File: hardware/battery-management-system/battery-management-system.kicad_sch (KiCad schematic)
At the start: 4 parts

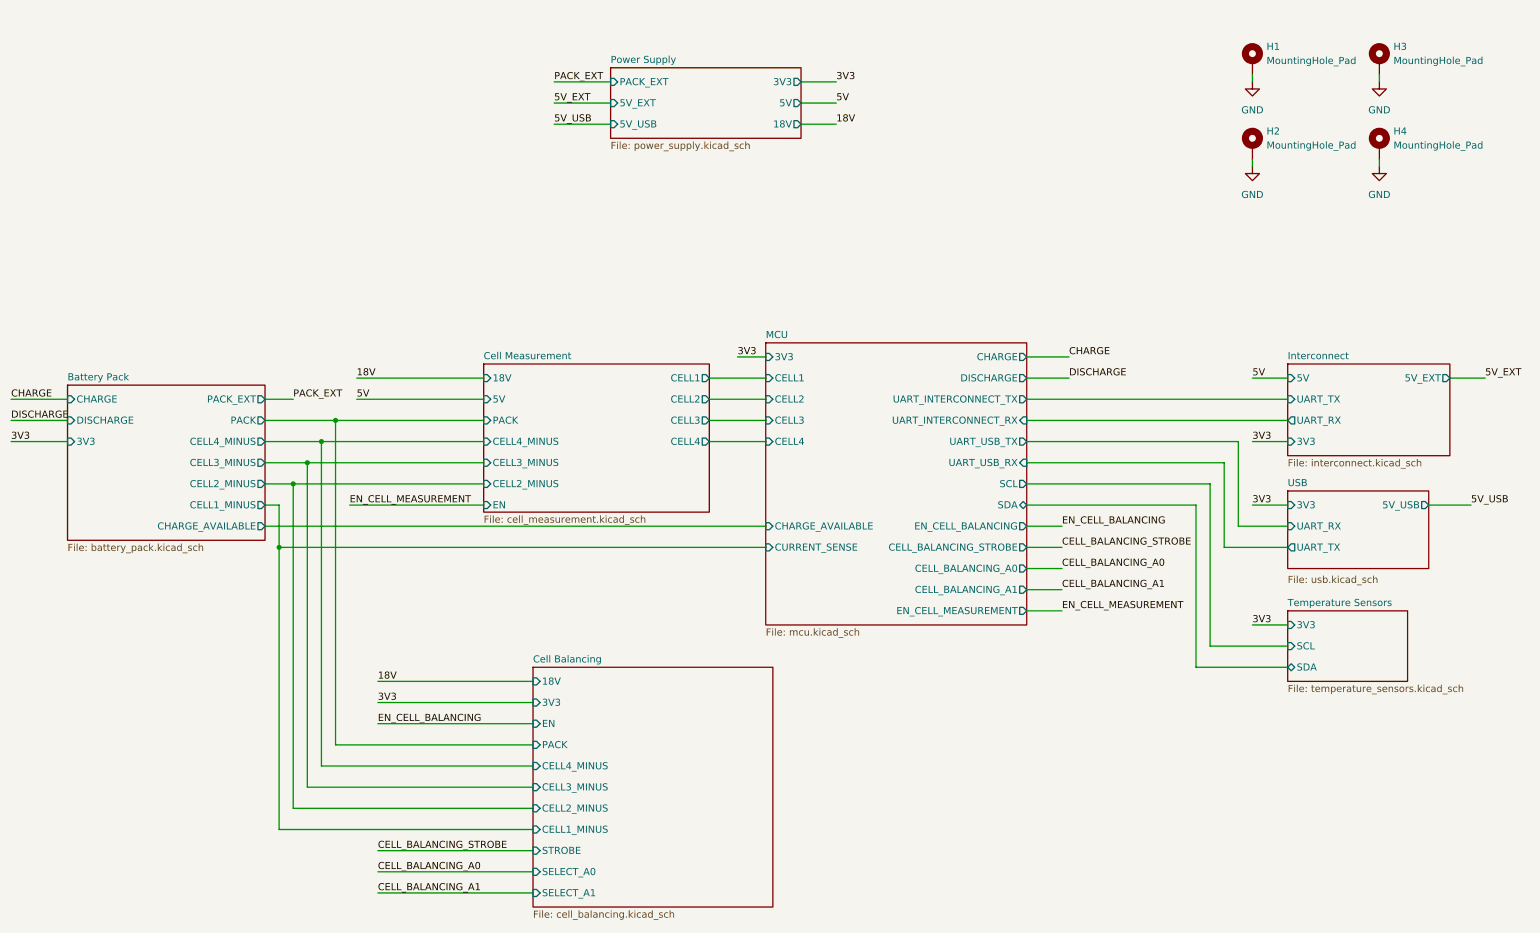
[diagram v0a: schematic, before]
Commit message: start simplifying BMS for R02
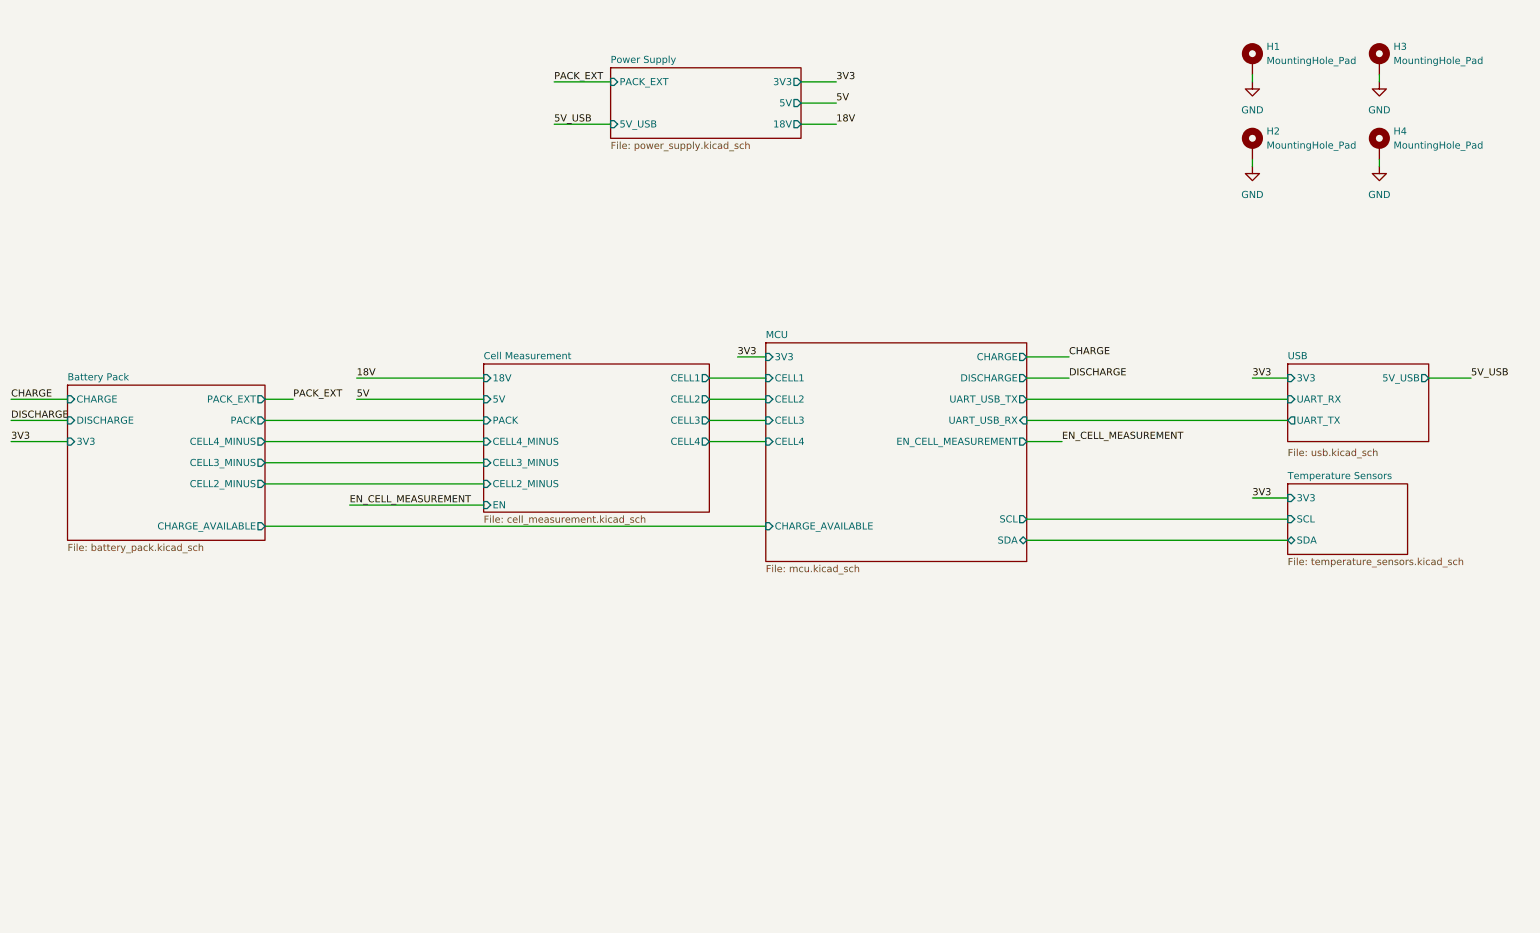
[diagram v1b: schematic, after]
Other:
- removed sheet Cell Balancing
- removed sheet Interconnect
- sheet Battery Pack ports: added none; removed CELL1_MINUS
- sheet MCU ports: added none; removed CELL_BALANCING_A0, CELL_BALANCING_A1, CELL_BALANCING_STROBE, CURRENT_SENSE, EN_CELL_BALANCING, UART_INTERCONNECT_RX, UART_INTERCONNECT_TX
- sheet Power Supply ports: added none; removed 5V_EXT

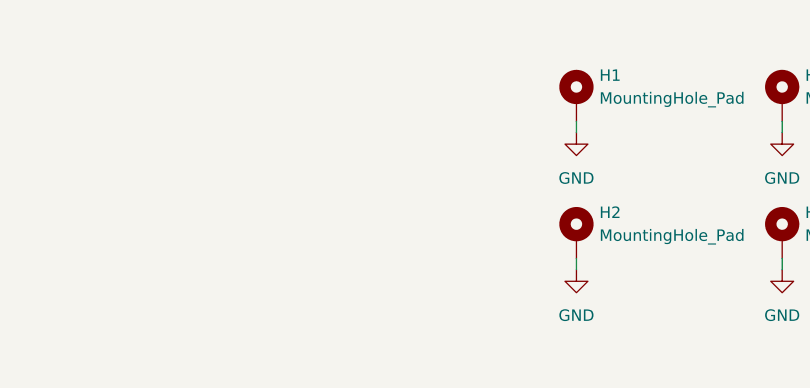
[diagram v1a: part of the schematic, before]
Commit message: add heatsink and fix ERC errors
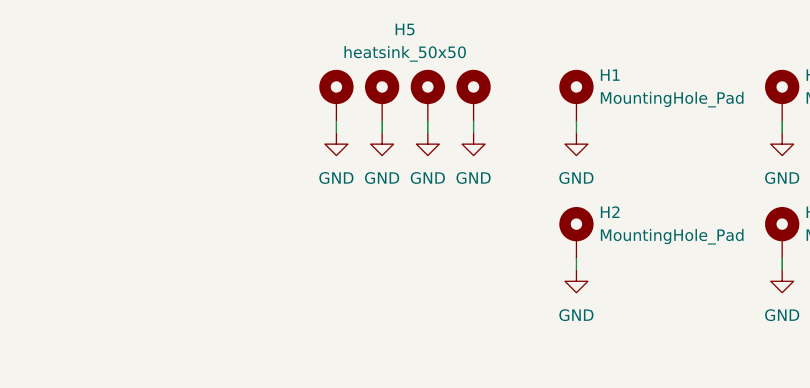
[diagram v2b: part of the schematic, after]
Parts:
- added H5: heatsink_50x50, benediktibk:heatsink_50x50, symbol benediktibk:heatsink_50x50
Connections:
- net GND: now also H5.1 (GND), H5.2 (GND), H5.3 (GND), H5.4 (GND)
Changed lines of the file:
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@@
+    (stroke (width 0) (type default))
+  )
+  (wire (pts (xy 209.55 25.4) (xy 209.55 26.67))
     (stroke (width 0) (type default))
   )
@@
     (stroke (width 0) (type default))
   )
+  (wire (pts (xy 219.71 25.4) (xy 219.71 26.67))
+    (stroke (width 0) (type default))
+  )
   (wire (pts (xy 74.93 80.01) (xy 97.79 80.01))
     (stroke (width 0) (type default))
@@
     (stroke (width 0) (type default))
   )
+  (wire (pts (xy 214.63 25.4) (xy 214.63 26.67))
+    (stroke (width 0) (type default))
+  )
   (wire (pts (xy 195.58 76.2) (xy 203.2 76.2))
     (stroke (width 0) (type default))
@@
     (stroke (width 0) (type default))
   )
+  (wire (pts (xy 224.79 25.4) (xy 224.79 26.67))
+    (stroke (width 0) (type default))
+  )
   (wire (pts (xy 195.58 83.82) (xy 242.57 83.82))
     (stroke (width 0) (type default))
@@
     )
   )
+  (symbol (lib_id "power:GND") (at 209.55 26.67 0) (unit 1)
+    (in_bom yes) (on_board yes) (dnp no) (fields_autoplaced)
+    (property "Reference" "#PWR067" (at 209.55 33.02 0)
+      (effects (font (size 1.27 1.27)) hide)
+    )
+    (property "Value" "GND" (at 209.55 31.75 0)
+      (effects (font (size 1.27 1.27)))
+    )
+    (property "Footprint" "" (at 209.55 26.67 0)
+      (effects (font (size 1.27 1.27)) hide)
+    )
+    (property "Datasheet" "" (at 209.55 26.67 0)
+      (effects (font (size 1.27 1.27)) hide)
+    )
+    (pin "1")
+    (instances
+      (project "battery-management-system"
+        (path "/5272f0ff-3069-41a9-bca2-80beede8b4b2"
+          (reference "#PWR067") (unit 1)
+        )
+      )
+    )
+  )
+  (symbol (lib_id "benediktibk:heatsink_50x50") (at 217.17 22.86 0) (unit 1)
+    (in_bom yes) (on_board yes) (dnp no) (fields_autoplaced)
+    (property "Reference" "H5" (at 217.17 15.24 0)
+      (effects (font (size 1.27 1.27)))
+    )
+    (property "Value" "heatsink_50x50" (at 217.17 17.78 0)
+      (effects (font (size 1.27 1.27)))
+    )
+    (property "Footprint" "benediktibk:heatsink_50x50" (at 217.297 12.954 0)
+      (effects (font (size 1.27 1.27)) hide)
+    )
+    (property "Datasheet" "~" (at 217.17 15.24 0)
+      (effects (font (size 1.27 1.27)) hide)
+    )
+    (pin "4")
+    (pin "1")
+    (pin "3")
+    (pin "2")
+    (instances
+      (project "battery-management-system"
+        (path "/5272f0ff-3069-41a9-bca2-80beede8b4b2"
+          (reference "H5") (unit 1)
+        )
+      )
+    )
+  )
   (symbol (lib_id "benediktibk:MountingHole_Pad_M6") (at 236.22 38.1 0) (unit 1)
     (in_bom yes) (on_board yes) (dnp no) (fields_autoplaced)
@@
     )
   )
+  (symbol (lib_id "power:GND") (at 224.79 26.67 0) (unit 1)
+    (in_bom yes) (on_board yes) (dnp no) (fields_autoplaced)
+    (property "Reference" "#PWR070" (at 224.79 33.02 0)
+      (effects (font (size 1.27 1.27)) hide)
+    )
+    (property "Value" "GND" (at 224.79 31.75 0)
+      (effects (font (size 1.27 1.27)))
+    )
+    (property "Footprint" "" (at 224.79 26.67 0)
+      (effects (font (size 1.27 1.27)) hide)
+    )
+    (property "Datasheet" "" (at 224.79 26.67 0)
+      (effects (font (size 1.27 1.27)) hide)
+    )
+    (pin "1")
+    (instances
+      (project "battery-management-system"
+        (path "/5272f0ff-3069-41a9-bca2-80beede8b4b2"
+          (reference "#PWR070") (unit 1)
+        )
+      )
+    )
+  )
+  (symbol (lib_id "power:GND") (at 214.63 26.67 0) (unit 1)
+    (in_bom yes) (on_board yes) (dnp no) (fields_autoplaced)
+    (property "Reference" "#PWR068" (at 214.63 33.02 0)
+      (effects (font (size 1.27 1.27)) hide)
+    )
+    (property "Value" "GND" (at 214.63 31.75 0)
+      (effects (font (size 1.27 1.27)))
+    )
+    (property "Footprint" "" (at 214.63 26.67 0)
+      (effects (font (size 1.27 1.27)) hide)
+    )
+    (property "Datasheet" "" (at 214.63 26.67 0)
+      (effects (font (size 1.27 1.27)) hide)
+    )
+    (pin "1")
+    (instances
+      (project "battery-management-system"
+        (path "/5272f0ff-3069-41a9-bca2-80beede8b4b2"
+          (reference "#PWR068") (unit 1)
+        )
+      )
+    )
+  )
   (symbol (lib_id "power:GND") (at 259.08 26.67 0) (unit 1)
     (in_bom yes) (on_board yes) (dnp no) (fields_autoplaced)
@@
         )
       )
+    )
+  )
+  (symbol (lib_id "power:GND") (at 219.71 26.67 0) (unit 1)
+    (in_bom yes) (on_board yes) (dnp no) (fields_autoplaced)
+    (property "Reference" "#PWR069" (at 219.71 33.02 0)
+      (effects (font (size 1.27 1.27)) hide)
+    )
+    (property "Value" "GND" (at 219.71 31.75 0)
+      (effects (font (size 1.27 1.27)))
+    )
+    (property "Footprint" "" (at 219.71 26.67 0)
+      (effects (font (size 1.27 1.27)) hide)
+    )
+    (property "Datasheet" "" (at 219.71 26.67 0)
+      (effects (font (size 1.27 1.27)) hide)
+    )
+    (pin "1")
+    (instances
+      (project "battery-management-system"
+        (path "/5272f0ff-3069-41a9-bca2-80beede8b4b2"
+          (reference "#PWR069") (unit 1)
+        )
+      )

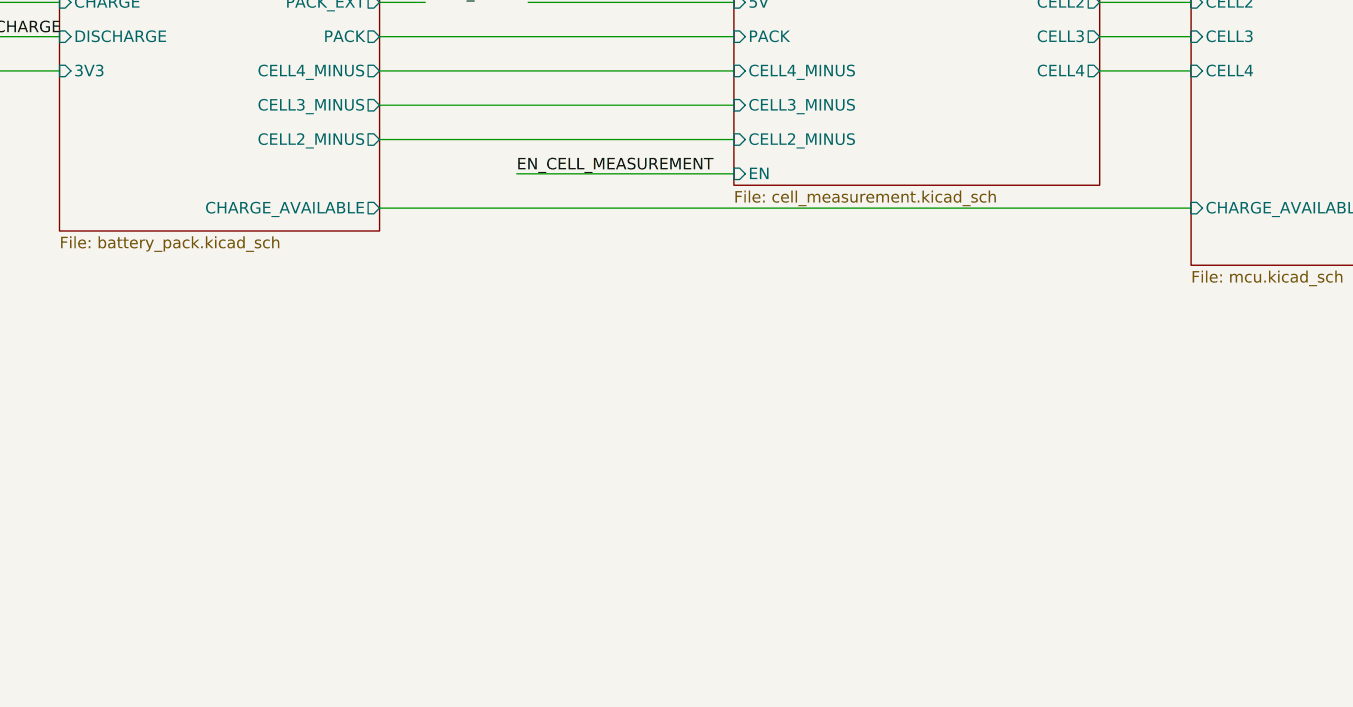
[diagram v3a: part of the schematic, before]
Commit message: add fuel gauge to BMS
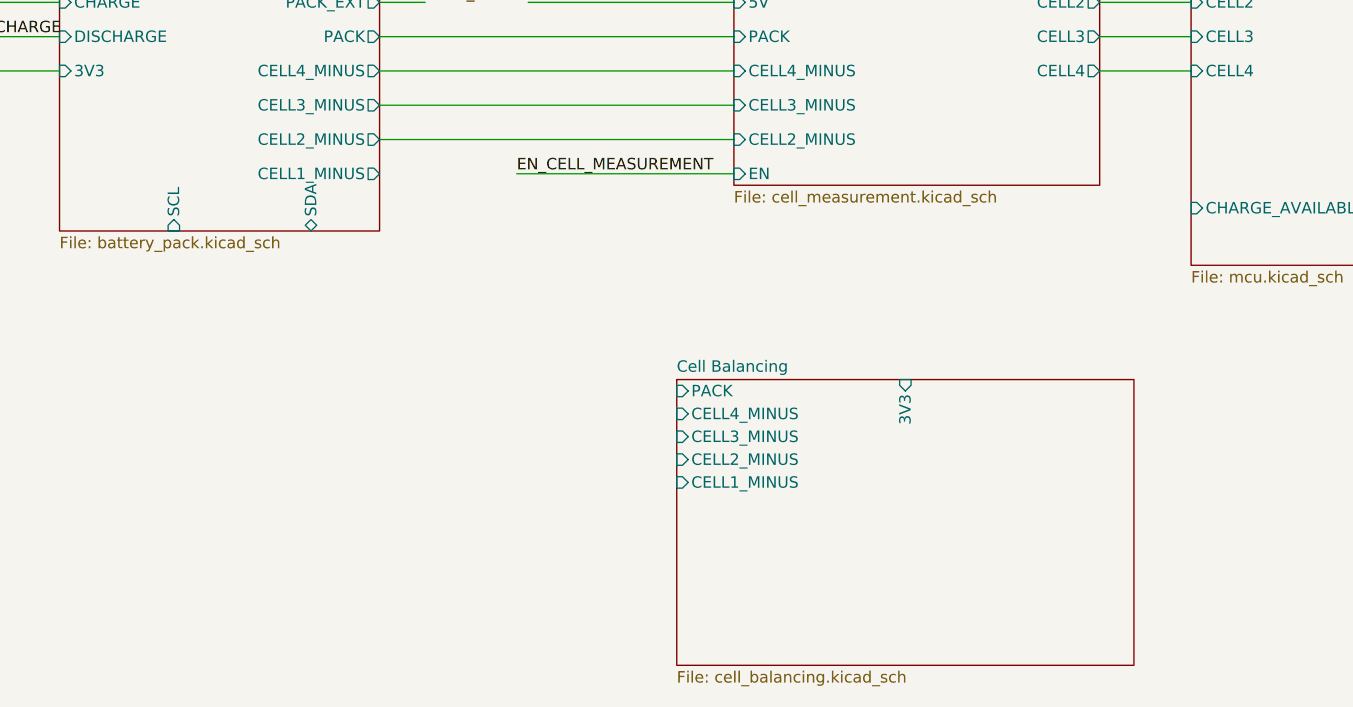
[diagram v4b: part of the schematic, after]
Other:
- added sheet Cell Balancing (cell_balancing.kicad_sch)
- sheet Battery Pack ports: added CELL1_MINUS, SCL, SDA; removed CHARGE_AVAILABLE
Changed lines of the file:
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@@
-	(wire
-		(pts
-			(xy 58.42 106.68) (xy 148.59 106.68)
-		)
-		(stroke
-			(width 0)
-			(type default)
-		)
-	)
 	(wire
 		(pts
@@
 	)
 	(sheet
+		(at 91.44 125.73)
+		(size 50.8 31.75)
+		(fields_autoplaced yes)
+		(stroke
+			(width 0.1524)
+			(type solid)
+		)
+		(fill
+			(color 0 0 0 0.0000)
+		)
+		(property "Sheetname" "Cell Balancing"
+			(at 91.44 125.0184 0)
+			(effects
+				(font
+					(size 1.27 1.27)
+				)
+				(justify left bottom)
+			)
+		)
+		(property "Sheetfile" "cell_balancing.kicad_sch"
+			(at 91.44 158.0646 0)
+			(effects
+				(font
+					(size 1.27 1.27)
+				)
+				(justify left top)
+			)
+		)
+		(pin "CELL3_MINUS" input
+			(at 91.44 132.08 180)
+			(effects
+				(font
+					(size 1.27 1.27)
+				)
+				(justify left)
+			)
+		)
+		(pin "CELL4_MINUS" input
+			(at 91.44 129.54 180)
+			(effects
+				(font
+					(size 1.27 1.27)
+				)
+				(justify left)
+			)
+		)
+		(pin "PACK" input
+			(at 91.44 127 180)
+			(effects
+				(font
+					(size 1.27 1.27)
+				)
+				(justify left)
+			)
+		)
+		(pin "CELL2_MINUS" input
+			(at 91.44 134.62 180)
+			(effects
+				(font
+					(size 1.27 1.27)
+				)
+				(justify left)
+			)
+		)
+		(pin "CELL1_MINUS" input
+			(at 91.44 137.16 180)
+			(effects
+				(font
+					(size 1.27 1.27)
+				)
+				(justify left)
+			)
+		)
+		(pin "3V3" input
+			(at 116.84 125.73 90)
+			(effects
+				(font
+					(size 1.27 1.27)
+				)
+				(justify right)
+			)
+		)
+		(instances
+			(project "battery-management-system"
+				(path "/5272f0ff-3069-41a9-bca2-80beede8b4b2"
+					(page "8")
+				)
+			)
+		)
+	)
+	(sheet
 		(at 22.86 81.28)
 		(size 35.56 27.94)
@@
 			)
 		)
-		(pin "CHARGE_AVAILABLE" output
-			(at 58.42 106.68 0)
-			(effects
-				(font
+		(pin "SDA" bidirectional
+			(at 50.8 109.22 270)
+			(effects
+				(font
+					(size 1.27 1.27)
+				)
+				(justify left)
+			)
+		)
+		(pin "SCL" input
+			(at 35.56 109.22 270)
+			(effects
+				(font
+					(size 1.27 1.27)
+				)
+				(justify left)
+			)
+		)
+		(pin "CELL1_MINUS" output
+			(at 58.42 102.87 0)
+			(effects
+				(font

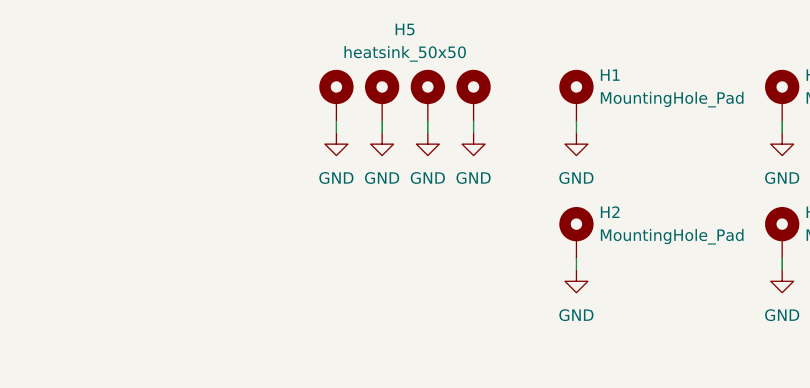
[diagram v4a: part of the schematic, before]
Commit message: fix design errors of battery management system R02
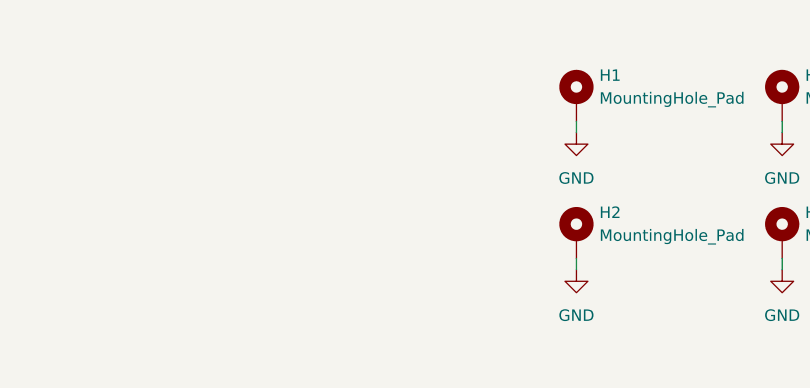
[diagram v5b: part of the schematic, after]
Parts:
- removed H5: heatsink_50x50, benediktibk:heatsink_50x50, symbol benediktibk:heatsink_50x50
